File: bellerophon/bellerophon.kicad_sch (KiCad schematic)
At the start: 35 parts, among them Q1 IRLL014NPBF, Q2 IRLL014NPBF, U1 Adafruit_ICM20948, U2 MPL3115A2, U3 Teensy4.0, U4 Adafruit SPI Flash SD Card

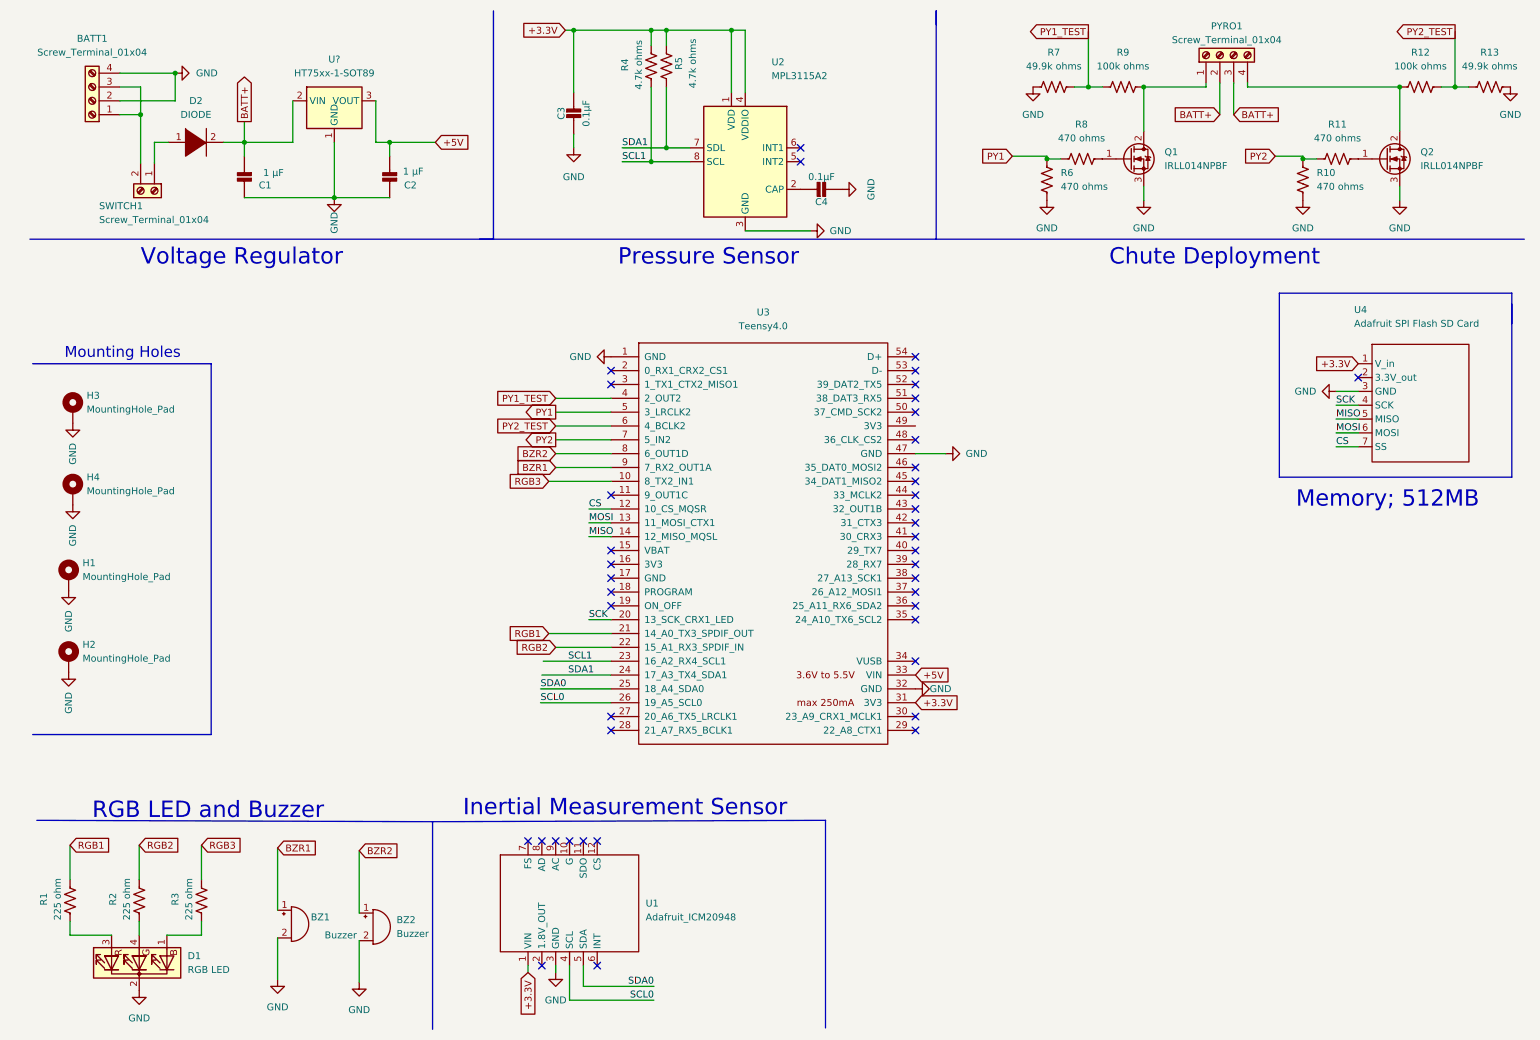
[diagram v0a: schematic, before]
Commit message: remove second battery input, combine battery and switch terminals into a single 1x4 terminal
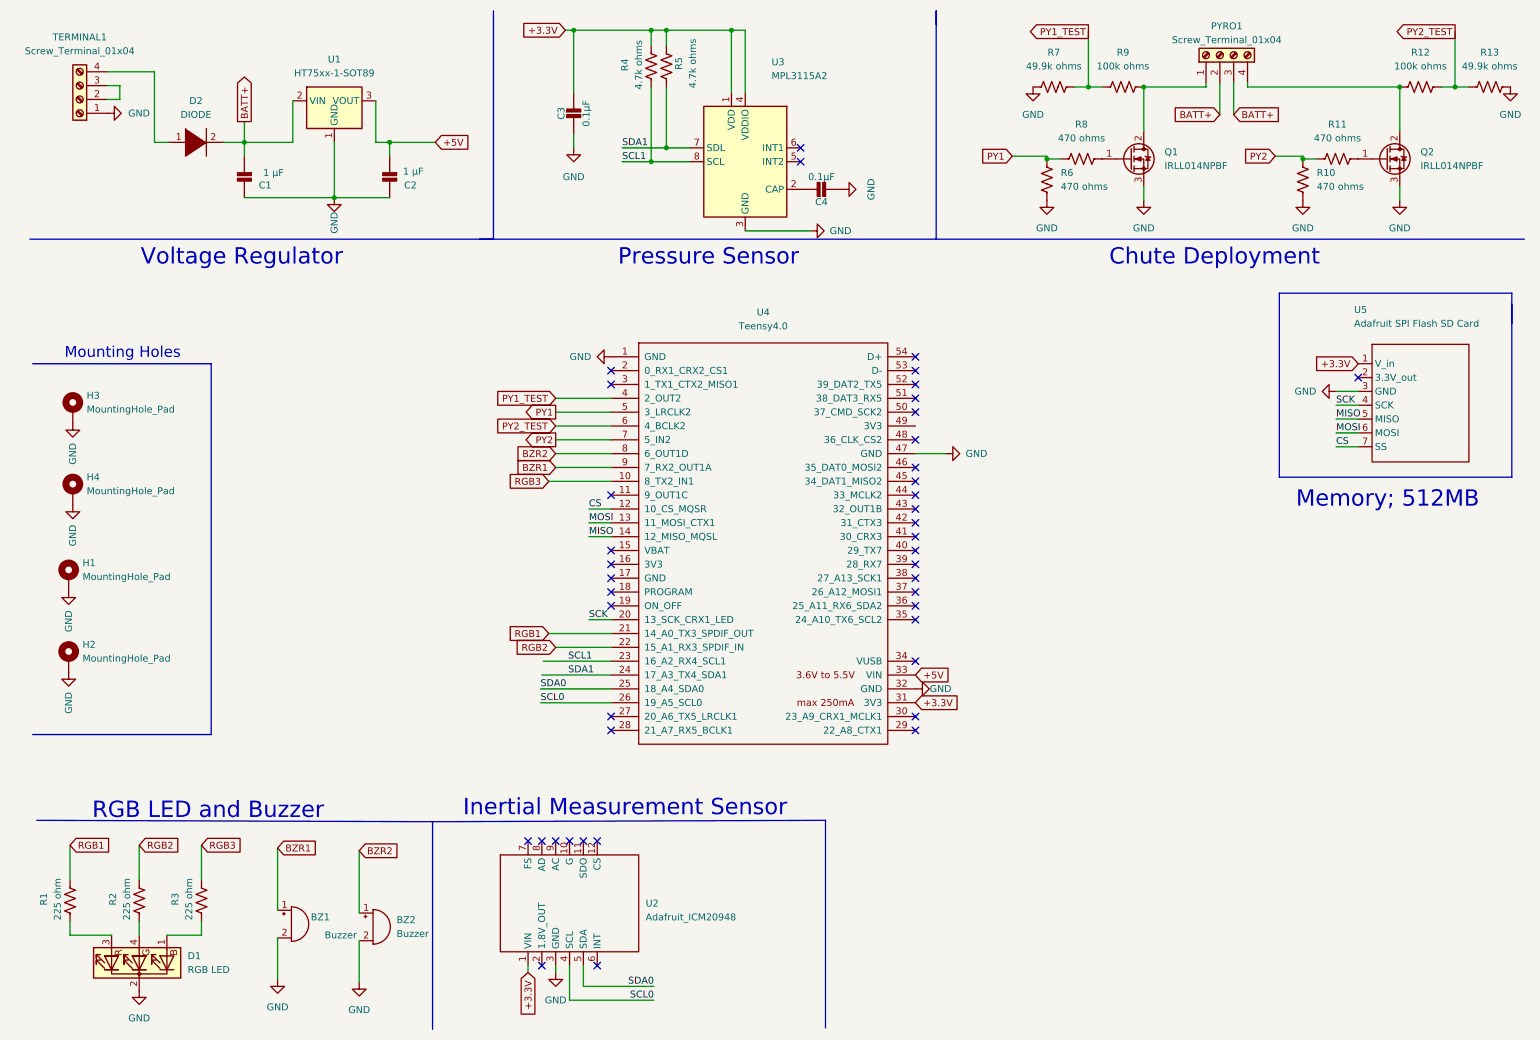
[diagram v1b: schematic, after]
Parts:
- removed SWITCH1: Screw_Terminal_01x04, RS-Components:SHDR2W105P0X500_1X2_1060X900X1250P, symbol Connector:Screw_Terminal_01x02
- gave numbers to parts that had none: 1
- renumbered BATT1 to TERMINAL1, U1 to U2, U2 to U3, U3 to U4, U4 to U5
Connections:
- net GND: now also TERMINAL1.1 (Pin_1); no longer TERMINAL1.2 (Pin_2), TERMINAL1.4 (Pin_4)
- net at D2.1 (K): now also TERMINAL1.4 (Pin_4)
- net at TERMINAL1.3 (Pin_3): now also TERMINAL1.2 (Pin_2); no longer TERMINAL1.1 (Pin_1)
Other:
- moved on the sheet: TERMINAL1

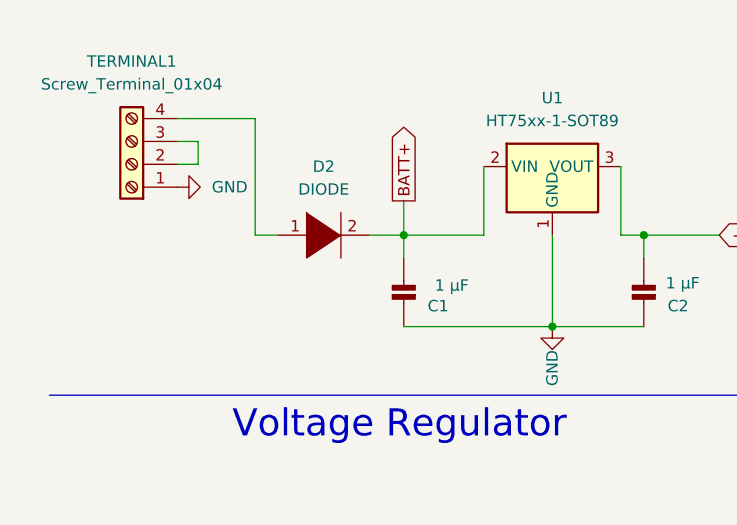
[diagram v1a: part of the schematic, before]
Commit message: replace switching diode with SMT PFET
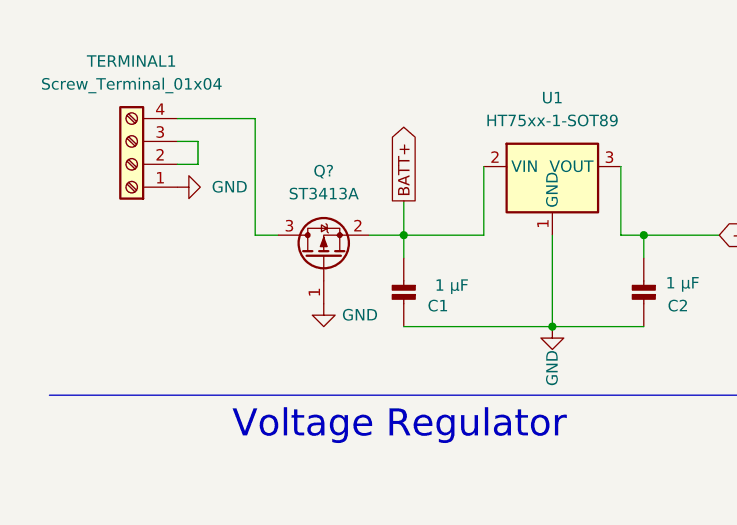
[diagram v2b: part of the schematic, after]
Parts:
- removed D2: DIODE, Diodes:D_P17.5mm_Horizontal, symbol pspice:DIODE
- added Q?: ST3413A, Package_TO_SOT_SMD:SOT-23, symbol Transistor_FET:TSM2301ACX
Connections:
- net BATT+: now also Q?.2 (S)
- net GND: now also Q?.1 (G)
- net at TERMINAL1.4 (Pin_4): now also Q?.3 (D)
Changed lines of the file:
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@@
     (pin "1")
+  )
+  (symbol (lib_id "Transistor_FET:TSM2301ACX") (at 41.91 38.1 90) (unit 1)
+    (in_bom yes) (on_board yes) (fields_autoplaced)
+    (property "Reference" "Q?" (id 0) (at 41.91 28.448 90))
+    (property "Value" "ST3413A" (id 1) (at 41.91 30.988 90))
+    (property "Footprint" "Package_TO_SOT_SMD:SOT-23" (id 2) (at 43.815 33.02 0)
+      (effects (font (size 1.27 1.27) italic) (justify left) hide)
+    )
+    (property "Datasheet" "https://www.taiwansemi.com/products/datasheet/TSM2301A_C15.pdf" (id 3) (at 41.91 38.1 0)
+      (effects (font (size 1.27 1.27)) (justify left) hide)
+    )
+    (pin "1")
+    (pin "2")
+    (pin "3")
   )
   (symbol (lib_id "power:GND") (at 67.31 45.72 0) (unit 1)
@@
     )
     (property "Datasheet" "" (id 3) (at 198.12 46.228 0)
+      (effects (font (size 1.27 1.27)) hide)
+    )
+    (pin "1")
+  )
+  (symbol (lib_id "power:GND") (at 41.91 43.18 0) (unit 1)
+    (in_bom yes) (on_board yes) (fields_autoplaced)
+    (property "Reference" "#PWR?" (id 0) (at 41.91 49.53 0)
+      (effects (font (size 1.27 1.27)) hide)
+    )
+    (property "Value" "GND" (id 1) (at 43.942 44.4499 0)
+      (effects (font (size 1.27 1.27)) (justify left))
+    )
+    (property "Footprint" "" (id 2) (at 41.91 43.18 0)
+      (effects (font (size 1.27 1.27)) hide)
+    )
+    (property "Datasheet" "" (id 3) (at 41.91 43.18 0)
       (effects (font (size 1.27 1.27)) hide)
     )
@@
     )
     (pin "1")
-  )
-  (symbol (lib_id "pspice:DIODE") (at 41.91 35.56 0) (unit 1)
-    (in_bom yes) (on_board yes) (fields_autoplaced)
-    (property "Reference" "D2" (id 0) (at 41.91 27.94 0))
-    (property "Value" "DIODE" (id 1) (at 41.91 30.48 0))
-    (property "Footprint" "Diodes:D_P17.5mm_Horizontal" (id 2) (at 41.91 35.56 0)
-      (effects (font (size 1.27 1.27)) hide)
-    )
-    (property "Datasheet" "~" (id 3) (at 41.91 35.56 0)
-      (effects (font (size 1.27 1.27)) hide)
-    )
-    (pin "1")
-    (pin "2")
   )
   (symbol (lib_id "Device:R_US") (at 199.39 25.4 90) (unit 1)
@@
       (reference "#PWR023") (unit 1) (value "GND") (footprint "")
     )
+    (path "/6da911ad-f54a-4fac-9f73-a6c4eb0e67f1"
+      (reference "#PWR?") (unit 1) (value "GND") (footprint "")
+    )
     (path "/8a393ed2-cfe0-4f0f-9490-ab6f8e39e2cc"
       (reference "BZ1") (unit 1) (value "Buzzer") (footprint "Buzzer:PiezoBuzzer-PS1240")
@@
       (reference "D1") (unit 1) (value "RGB LED") (footprint "LED_THT:LED_D5.0mm-4_RGB")
     )
-    (path "/da123791-e238-4fc2-a356-0eeba872e986"
-      (reference "D2") (unit 1) (value "DIODE") (footprint "Diodes:D_P17.5mm_Horizontal")
-    )
     (path "/737af3b0-bc82-4c4d-8cad-6c0d629637f8"
       (reference "H1") (unit 1) (value "MountingHole_Pad") (footprint "MountingHole:MountingHole_2.2mm_M2_Pad")
@@
       (reference "Q2") (unit 1) (value "IRLL014NPBF") (footprint "Package_TO_SOT_SMD:SOT-223-3_TabPin2")
     )
+    (path "/43963cea-368b-4863-85f3-8f5acb306b53"
+      (reference "Q?") (unit 1) (value "ST3413A") (footprint "Package_TO_SOT_SMD:SOT-23")
+    )
     (path "/b5e0014b-e7da-426b-94bd-146b6879c8aa"

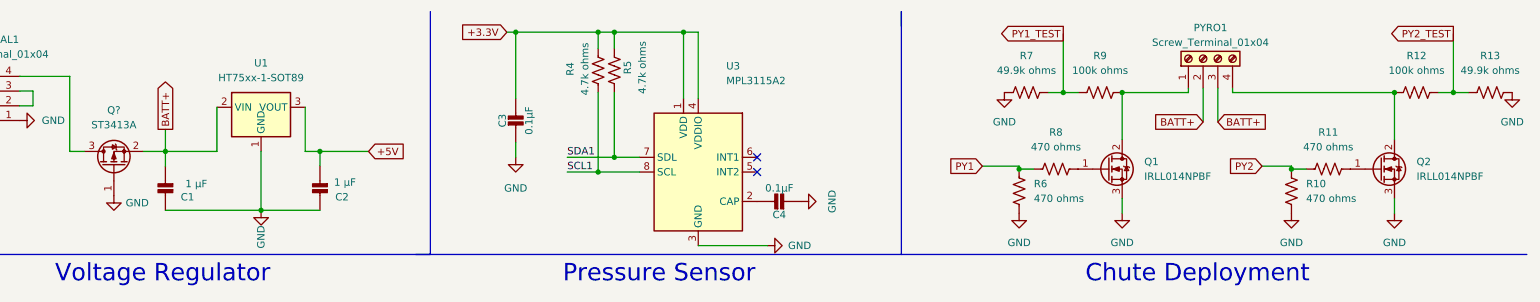
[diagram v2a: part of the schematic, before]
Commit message: correct name on voltage regulator
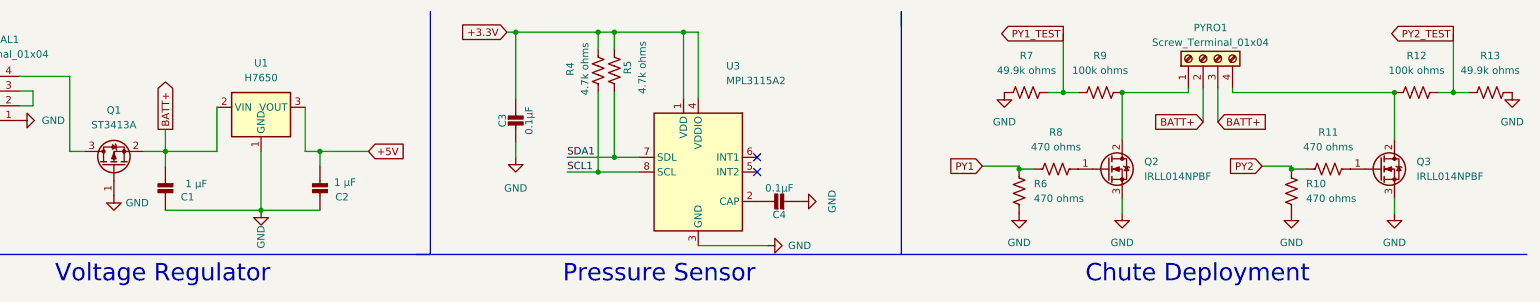
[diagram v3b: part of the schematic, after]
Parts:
- U1: value HT75xx-1-SOT89 -> H7650
- gave numbers to parts that had none: 1
- renumbered Q1 to Q2, Q2 to Q3

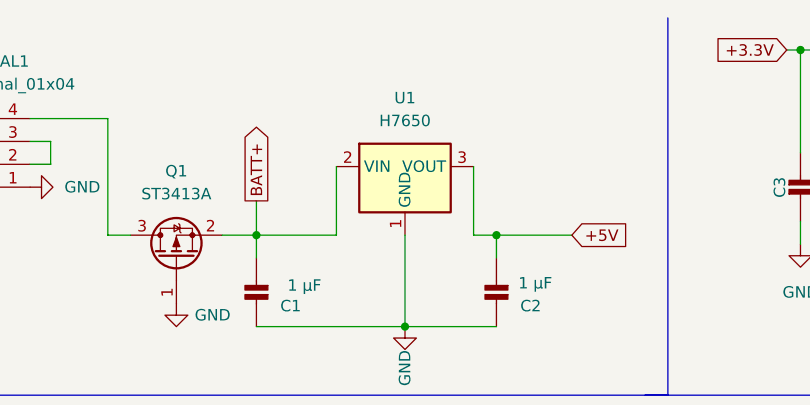
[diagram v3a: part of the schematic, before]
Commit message: add datasheets, change regulator to a ht7350-a
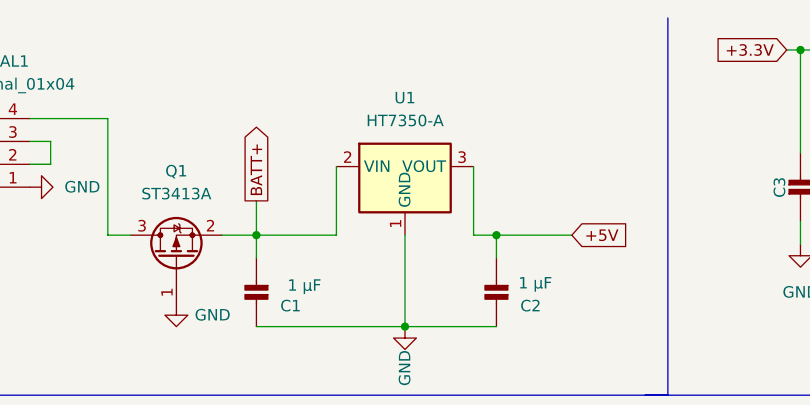
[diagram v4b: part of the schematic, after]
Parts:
- U1: value H7650 -> HT7350-A
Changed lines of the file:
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@@
     (in_bom yes) (on_board yes) (fields_autoplaced)
     (property "Reference" "U1" (id 0) (at 67.31 20.32 0))
-    (property "Value" "H7650" (id 1) (at 67.31 22.86 0))
+    (property "Value" "HT7350-A" (id 1) (at 67.31 22.86 0))
     (property "Footprint" "Package_TO_SOT_SMD:SOT-89-3" (id 2) (at 67.31 22.225 0)
       (effects (font (size 1.27 1.27) italic) hide)
@@
     )
     (path "/ba39f310-23c5-4a56-baa7-cf88b08d466d"
-      (reference "U1") (unit 1) (value "H7650") (footprint "Package_TO_SOT_SMD:SOT-89-3")
+      (reference "U1") (unit 1) (value "HT7350-A") (footprint "Package_TO_SOT_SMD:SOT-89-3")
     )
     (path "/1c61f331-fa92-48e1-9819-ab0be4ebf718"

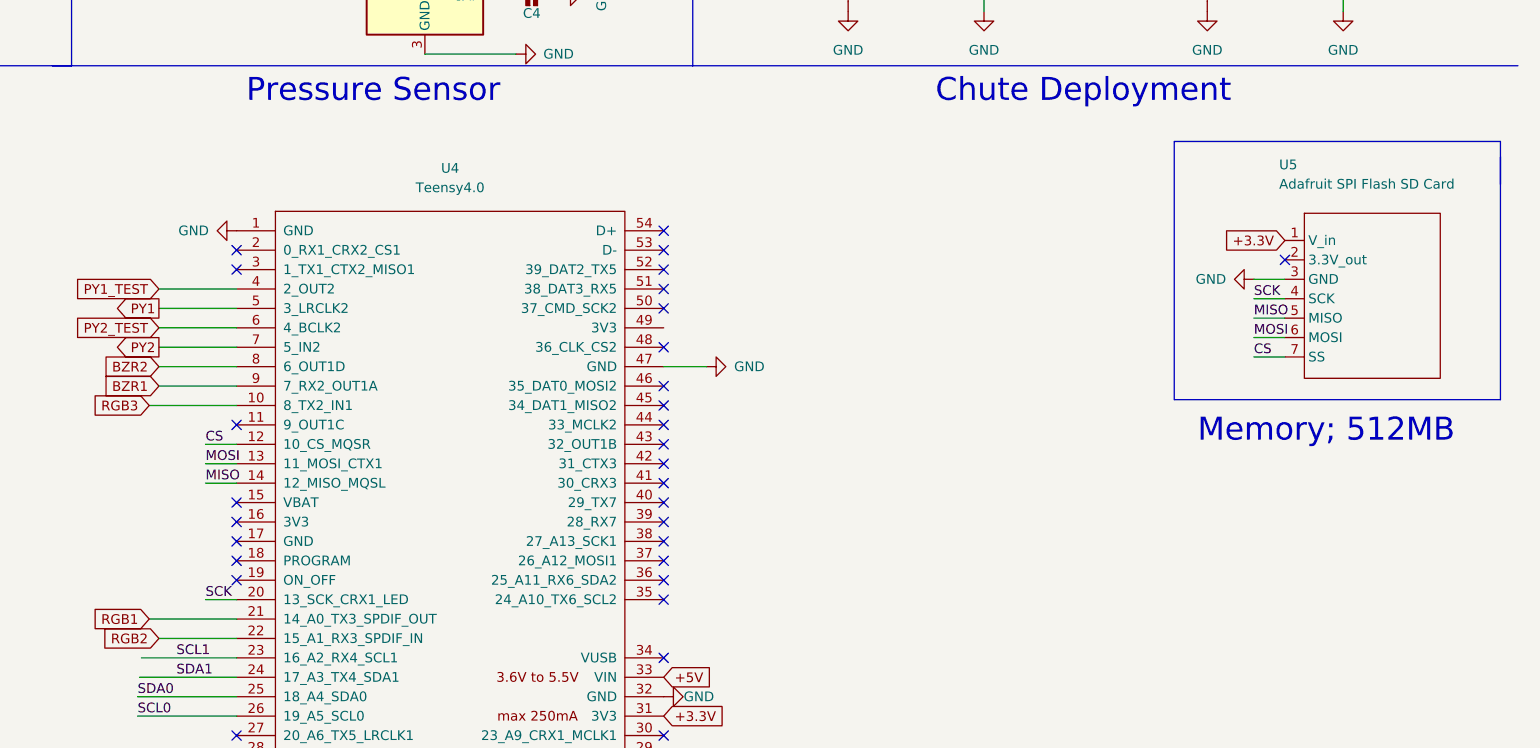
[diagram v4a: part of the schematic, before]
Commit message: SD breakout convert to surface mount
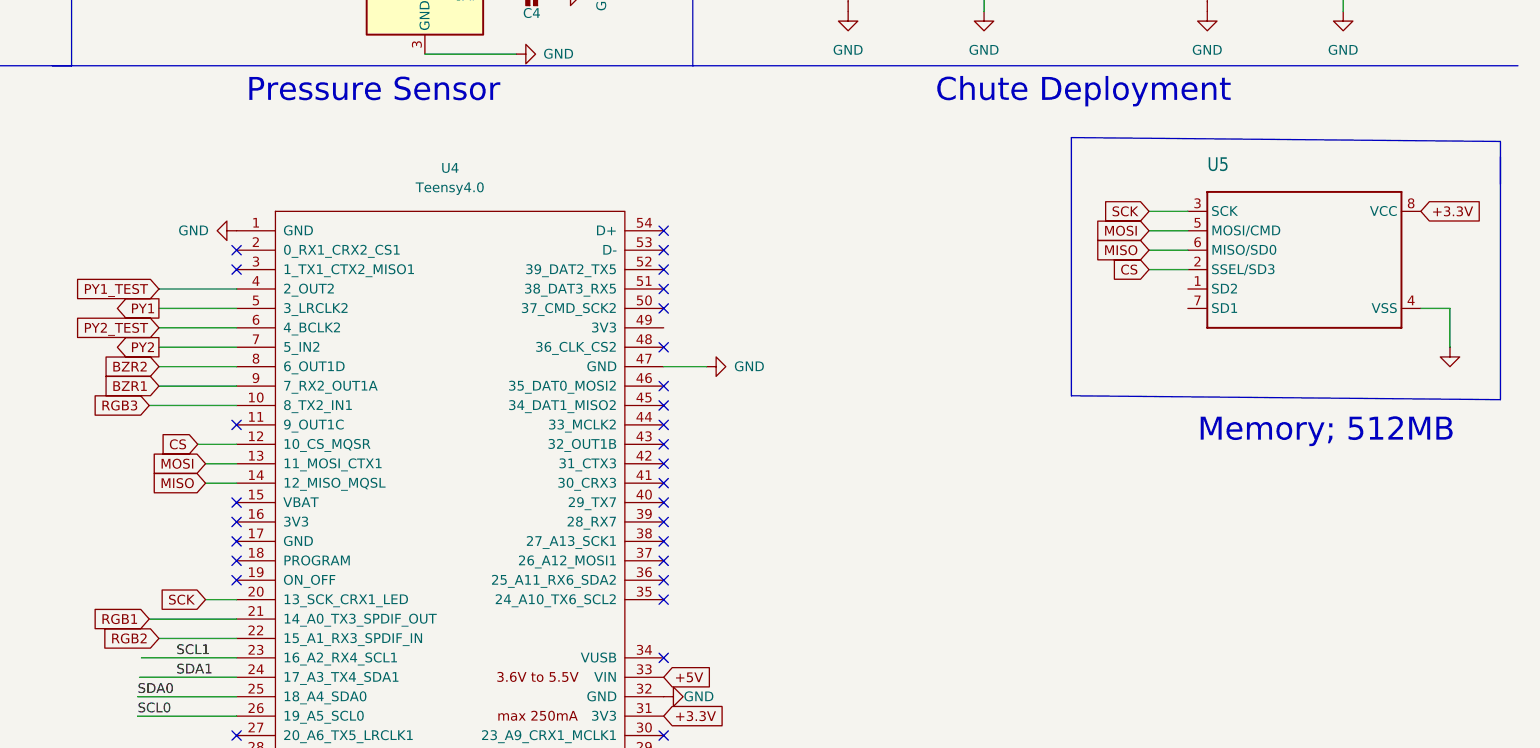
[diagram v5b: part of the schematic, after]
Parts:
- removed U5: Adafruit SPI Flash SD Card, Adafruit:SD-CARD-B21.59x17.78mm-1X07_ROUND_70-P2.5mm, symbol Adafruit:Adafruit SPI Flash SD Card
- added U5: (no value), symbol Adafruit SPI Flash SD Card-eagle-import:SMT_SDCARD_8PIN
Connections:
- net +3.3V: now also U5.8 (VCC)
- net CS: now also U5.2 (SSEL/SD3)
- net GND: now also U5.4 (VSS)
- net MISO: now also U5.6 (MISO/SD0)
- net MOSI: now also U5.5 (MOSI/CMD)
- net SCK: now also U5.3 (SCK)
- no-connect marks 42 -> 41
